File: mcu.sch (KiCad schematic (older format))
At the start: 64 parts, among them J3 SWD, P1 USB_C_Plug_USB2.0, Q1 AO3401A, U10 USBLC6-2SC6, U11 MCP2551-I-SN, U12 STM32F429ZGTx, U8 TPS5430DDA, U9 TPS5430DDA, Y1 25mhz

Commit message: Layout p much finished.. Time for some stretch goals..?
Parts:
- removed C42: 100n, Capacitor_SMD:C_0402_1005Metric_Pad0.74x0.62mm_HandSolder, symbol Device:C_Small
- removed P1: USB_C_Plug_USB2.0, Connector_USB:USB_C_Receptacle_Amphenol_12401548E4-2A, symbol Connector:USB_C_Plug_USB2.0
- removed R48, R51: 5.1k, Resistor_SMD:R_0402_1005Metric_Pad0.72x0.64mm_HandSolder, symbol Device:R_Small
- removed R49, R50: 22, Resistor_SMD:R_0402_1005Metric_Pad0.72x0.64mm_HandSolder, symbol Device:R_Small
- added J4: USB_B, Connector_USB:USB_B_Amphenol_MUSB-D511_Vertical_Rugged, symbol Connector:USB_B
- added J5: USB_EXT, Connector_PinHeader_2.54mm:PinHeader_1x05_P2.54mm_Vertical_SMD_Pin1Left, symbol Connector:Conn_01x05_Male
- added TP18: TP_BUCK_EN, TestPoint:TestPoint_Pad_D1.0mm, symbol Connector:TestPoint_Small
- added TP19: TP_PWR_GND2, TestPoint:TestPoint_Pad_D1.0mm, symbol Connector:TestPoint_Small
- added TP20: TP_PWR_GND1, TestPoint:TestPoint_Pad_D1.0mm, symbol Connector:TestPoint_Small
- added TP21: TP_BUCK_IN, TestPoint:TestPoint_Pad_D1.0mm, symbol Connector:TestPoint_Small
- TP10: value TestPoint_Small -> TP_5V
- TP11: value TestPoint_Small -> TP_3V
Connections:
- net labels added: USB_CONN_SHIELD
- wire segments 230 -> 226
- no-connect marks 3 -> 2

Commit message: Update Schematic with a bunch of extra stuff
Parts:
- added C42, C52: 12p, Capacitor_SMD:C_0402_1005Metric_Pad0.74x0.62mm_HandSolder, symbol Device:C_Small
- added C53: 10u, Capacitor_SMD:C_0402_1005Metric_Pad0.74x0.62mm_HandSolder, symbol Device:C_Small
- added C54: 100n, Capacitor_SMD:C_0402_1005Metric_Pad0.74x0.62mm_HandSolder, symbol Device:C_Small
- added C? (x3): 0.1u, Capacitor_SMD:C_1206_3216Metric_Pad1.33x1.80mm_HandSolder, symbol Device:C_Small
- added C?: 47u, Capacitor_SMD:CP_Elec_5x5.8, symbol Device:CP_Small
- added C?: 10u, Capacitor_Tantalum_SMD:CP_EIA-7343-20_Kemet-V_Pad2.25x2.55mm_HandSolder, symbol Device:CP_Small
- added D22, D25, D26, D27, D28, D29, D30: ESD9B3.3ST5G, Diode_SMD:D_SOD-923, symbol Diode:ESD9B3.3ST5G
- added D23: PWR_5V_GREEN, LED_SMD:LED_0603_1608Metric_Pad1.05x0.95mm_HandSolder, symbol Device:LED_Small
- added D24: PWR_3V_RED, LED_SMD:LED_0603_1608Metric_Pad1.05x0.95mm_HandSolder, symbol Device:LED_Small
- added D? (x2): MM3Zxx, Diode_SMD:D_SOD-323_HandSoldering, symbol Device:D_Small
- added J6: Micro_SD_Card_Det, Connector_Card:microSD_HC_Molex_104031-0811, symbol Connector:Micro_SD_Card_Det
- added J?: HC-05, Connector_PinHeader_2.54mm:PinHeader_1x06_P2.54mm_Vertical, symbol Connector_Generic:Conn_01x06
- added R48: 47, Resistor_SMD:R_0402_1005Metric_Pad0.72x0.64mm_HandSolder, symbol Device:R_Small
- added R49, R74, R75: null, Resistor_SMD:R_0603_1608Metric_Pad0.98x0.95mm_HandSolder, symbol Device:R_Small
- added R50, R51: 4.7k, Resistor_SMD:R_0603_1608Metric_Pad0.98x0.95mm_HandSolder, symbol Device:R_Small
- added R73, R76, R77, R78, R79: 10k, Resistor_SMD:R_0603_1608Metric_Pad0.98x0.95mm_HandSolder, symbol Device:R_Small
- added RV?: Varistor, Varistor:RV_Disc_D15.5mm_W3.9mm_P7.5mm, symbol Device:Varistor
- added TP?: TP_VPROT, TestPoint:TestPoint_Pad_D1.0mm, symbol Connector:TestPoint_Small
- added U16: ATECC608A-SSHDA, Package_SO:SOIC-8_3.9x4.9mm_P1.27mm, symbol Security:ATECC608A-SSHDA
- added Y2: Crystal, Crystal:Crystal_SMD_3215-2Pin_3.2x1.5mm, symbol Device:Crystal
- R53: value 3.24k -> null
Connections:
- net +3V3: now also C54.1, R49.1, R50.2, R51.2, R74.2, R76.2, R77.2, R78.2, R79.2, U16.8 (VCC); no longer C23.1, U11.3 (VDD), U11.5 (Vref)
- net +5V: now also C23.1, U11.3 (VDD), U11.5 (Vref), C?.1, C?.1, C?.1, D?.1 (K), J?.2 (Pin_2), R75.2, TP?.1
- net 12v-SW: now also C?.1, C?.1, D?.2 (A), RV?.2
- net GND: now also C42.2, C52.2, C53.1, C54.2, C?.2, C?.2, C?.2, C?.2, C?.2, D22.2 (A2), D23.1 (K), D24.1 (K), D25.2 (A2), D26.2 (A2), D27.2 (A2), D28.2 (A2), D29.2 (A2), D30.2 (A2), D?.2 (A), J6.6 (VSS), J?.3 (Pin_3), RV?.1, U16.4 (GND)
- net HSE_IN: now also R48.2
- net HSE_OUT: now also C42.1, Y2.1
- net MCU-CLUTCH: now also U12.73 (PB12); no longer U12.76 (PB15)
- net MCU-CRNK: now also U12.118 (PD4); no longer U12.116 (PD2)
- net MCU-IAT: now also U12.46 (PB0); no longer U12.34 (PA0)
- net MCU-IGN-1: now also U12.34 (PA0); no longer U12.96 (PC6)
- net MCU-IGN-2: now also U12.35 (PA1); no longer U12.97 (PC7)
- net MCU-IGN-3: now also U12.69 (PB10); no longer U12.46 (PB0)
- net MCU-IGN-4: now also U12.70 (PB11); no longer U12.47 (PB1)
- net MCU-RN1: now also U12.101 (PA9); no longer U12.69 (PB10)
- net MCU-RN2: now also U12.102 (PA10); no longer U12.70 (PB11)
- net MCU-TPS: now also U12.47 (PB1); no longer U12.35 (PA1)
- net UART7_RX: now also J?.5 (Pin_5)
- net UART7_TX: now also J?.4 (Pin_4)
- net USB_CONN_SHIELD: now also J6.11 (SHIELD)
- net MCU-CEL: now reaches U12.100 (PA8)
- net SDIO_D2: now reaches U12.111 (PC10)
- net SDIO_D2: now also D26.1 (A1), J6.1 (DAT2), R78.1
- net SDIO_D3: now reaches U12.112 (PC11)
- net SDIO_D3: now also D27.1 (A1), J6.2 (DAT3/CD)
- net SDIO_CK: now reaches U12.113 (PC12)
- net SDIO_CK: now also D29.1 (A1), J6.5 (CLK)
- net I2C1_SDL: now reaches U12.136 (PB6)
- net I2C1_SDL: now also R51.1, U16.6 (SCL)
- net I2C1_SDA: now reaches U12.137 (PB7)
- net I2C1_SDA: now also R50.1, U16.5 (SDA)
- net MCU-PWM2: now reaches U12.4 (PE5)
- net MCU-PWM3: now reaches U12.5 (PE6)
- net LSE_IN: now reaches U12.8 (PC14)
- net MCU-VVT: now reaches U12.81 (PD12)
- net MCU-PWM1: now reaches U12.82 (PD13)
- net MCU-ANALOG-1: now reaches U12.87 (PG2)
- net MCU-ANALOG-2: now reaches U12.88 (PG3)
- net MCU-ANALOG-3: now reaches U12.89 (PG4)
- net LSE_OUT: now reaches U12.9 (PC15)
- net MCU-ANALOG-4: now reaches U12.90 (PG5)
- net SDIO_D0: now reaches U12.98 (PC8)
- net SDIO_D0: now also D22.1 (A1), J6.7 (DAT0), R76.1
- net SDIO_D1: now reaches U12.99 (PC9)
- net SDIO_D1: now also D25.1 (A1), J6.8 (DAT1), R77.1
- net MCU-BARO renamed MCU-EXT-MAP
- new net: C52.1, R48.1, Y2.2
- new net: D23.2 (A), R74.1
- new net: D24.2 (A), R75.1
- new net SDIO_CMD: D28.1 (A1), J6.3 (CMD), R73.2, R79.1, U12.116 (PD2)
- new net SDIO_VDD: C53.2, D30.1 (A1), J6.4 (VDD), R49.2, R73.1
- new net VREG: D?.1 (K)
- no-connect marks 2 -> 6
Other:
- note added: "ATECCA"
- note added: "HC-05"
- note added: "POWER LEDS\n"
- note added: "SDCARD + ESD"
- moved on the sheet: C23, C27, C28, C29, C30, C31, C32, C33, C34, C35, C36, C37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

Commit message: Start rerouting again
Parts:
- J4: footprint Connector_USB:USB_B_Amphenol_MUSB-D511_Vertical_Rugged -> Connector_USB:USB_B_Lumberg_2411_02_Horizontal
- gave numbers to parts that had none: 10
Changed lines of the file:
@@
 F 0 "J4" H 1757 7567 50  0000 C CNN
 F 1 "USB_B" H 1757 7476 50  0000 C CNN
-F 2 "Connector_USB:USB_B_Amphenol_MUSB-D511_Vertical_Rugged" H 1850 7050 50  0001 C CNN
+F 2 "Connector_USB:USB_B_Lumberg_2411_02_Horizontal" H 1850 7050 50  0001 C CNN
 F 3 " ~" H 1850 7050 50  0001 C CNN
 	1    1700 7100
@@
 NoConn ~ 13200 5650
 $Comp
-L Connector_Generic:Conn_01x06 J?
+L Connector_Generic:Conn_01x06 J7
 U 1 1 61A6A58F
 P 3250 10850
-F 0 "J?" H 3168 10325 50  0000 C CNN
+F 0 "J7" H 3168 10325 50  0000 C CNN
 F 1 "HC-05" H 3168 10416 50  0000 C CNN
 F 2 "Connector_PinHeader_2.54mm:PinHeader_1x06_P2.54mm_Vertical" H 3250 10850 50  0001 C CNN
@@
 UART7_TX
 $Comp
-L power:GND #PWR?
+L power:GND #PWR092
 U 1 1 61A7105A
 P 3900 10850
-F 0 "#PWR?" H 3900 10600 50  0001 C CNN
+F 0 "#PWR092" H 3900 10600 50  0001 C CNN
 F 1 "GND" H 3905 10677 50  0000 C CNN
 F 2 "" H 3900 10850 50  0001 C CNN
@@
 P 3950 10950
 AR Path="/61A87E29" Ref="#PWR?"  Part="1"
-AR Path="/608F155A/61A87E29" Ref="#PWR?"  Part="1"
-F 0 "#PWR?" H 3950 10800 50  0001 C CNN
+AR Path="/608F155A/61A87E29" Ref="#PWR093"  Part="1"
+F 0 "#PWR093" H 3950 10800 50  0001 C CNN
 F 1 "+5V" V 3950 11050 50  0000 L CNN
 F 2 "" H 3950 10950 50  0001 C CNN
@@
 P 4850 1300
 AR Path="/5F2C75FB/61BA4550" Ref="RV?"  Part="1"
-AR Path="/608F155A/61BA4550" Ref="RV?"  Part="1"
-F 0 "RV?" H 4729 1254 50  0000 R CNN
+AR Path="/608F155A/61BA4550" Ref="RV1"  Part="1"
+F 0 "RV1" H 4729 1254 50  0000 R CNN
 F 1 "Varistor" H 4729 1345 50  0000 R CNN
 F 2 "Varistor:RV_Disc_D15.5mm_W3.9mm_P7.5mm" V 4780 1300 50  0001 C CNN
@@
 P 5650 1350
 AR Path="/5F2C75FB/61BA4558" Ref="C?"  Part="1"
-AR Path="/608F155A/61BA4558" Ref="C?"  Part="1"
-F 0 "C?" H 5742 1396 50  0000 L CNN
+AR Path="/608F155A/61BA4558" Ref="C59"  Part="1"
+F 0 "C59" H 5742 1396 50  0000 L CNN
 F 1 "0.1u" H 5742 1305 50  0000 L CNN
 F 2 "Capacitor_SMD:C_1206_3216Metric_Pad1.33x1.80mm_HandSolder" H 5650 1350 50  0001 C CNN
@@
 P 5950 950
 AR Path="/5F2C75FB/61BA4563" Ref="D?"  Part="1"
-AR Path="/608F155A/61BA4563" Ref="D?"  Part="1"
-F 0 "D?" H 5950 743 50  0000 C CNN
+AR Path="/608F155A/61BA4563" Ref="D35"  Part="1"
+F 0 "D35" H 5950 743 50  0000 C CNN
 F 1 "MM3Zxx" H 5950 834 50  0000 C CNN
 F 2 "Diode_SMD:D_SOD-323_HandSoldering" V 5950 950 50  0001 C CNN
@@
 P 5500 3600
 AR Path="/5F2C75FB/61BA4578" Ref="C?"  Part="1"
-AR Path="/608F155A/61BA4578" Ref="C?"  Part="1"
-F 0 "C?" H 5592 3646 50  0000 L CNN
+AR Path="/608F155A/61BA4578" Ref="C58"  Part="1"
+F 0 "C58" H 5592 3646 50  0000 L CNN
 F 1 "0.1u" H 5592 3555 50  0000 L CNN
 F 2 "Capacitor_SMD:C_1206_3216Metric_Pad1.33x1.80mm_HandSolder" H 5500 3600 50  0001 C CNN
@@
 P 5150 3550
 AR Path="/5F2C75FB/61BA4580" Ref="C?"  Part="1"
-AR Path="/608F155A/61BA4580" Ref="C?"  Part="1"
-F 0 "C?" H 5238 3596 50  0000 L CNN
+AR Path="/608F155A/61BA4580" Ref="C56"  Part="1"
+F 0 "C56" H 5238 3596 50  0000 L CNN
 F 1 "47u" H 5238 3505 50  0000 L CNN
 F 2 "Capacitor_SMD:CP_Elec_5x5.8" H 5150 3550 50  0001 C CNN
@@
 P 4700 3550
 AR Path="/5F2C75FB/61BA4588" Ref="D?"  Part="1"
-AR Path="/608F155A/61BA4588" Ref="D?"  Part="1"
-F 0 "D?" V 4654 3620 50  0000 L CNN
+AR Path="/608F155A/61BA4588" Ref="D34"  Part="1"
+F 0 "D34" V 4654 3620 50  0000 L CNN
 F 1 "MM3Zxx" V 4745 3620 50  0000 L CNN
 F 2 "Diode_SMD:D_SOD-323_HandSoldering" V 4700 3550 50  0001 C CNN
@@
 P 5350 1350
 AR Path="/5F2C75FB/61BA459E" Ref="C?"  Part="1"
-AR Path="/608F155A/61BA459E" Ref="C?"  Part="1"
-F 0 "C?" H 5438 1396 50  0000 L CNN
+AR Path="/608F155A/61BA459E" Ref="C57"  Part="1"
+F 0 "C57" H 5438 1396 50  0000 L CNN
 F 1 "10u" H 5438 1305 50  0000 L CNN
 F 2 "Capacitor_Tantalum_SMD:CP_EIA-7343-20_Kemet-V_Pad2.25x2.55mm_HandSolder" H 5350 1350 50  0001 C CNN
@@
 P 5850 3600
 AR Path="/5F2C75FB/61BA45A9" Ref="C?"  Part="1"
-AR Path="/608F155A/61BA45A9" Ref="C?"  Part="1"
-F 0 "C?" H 5942 3646 50  0000 L CNN
+AR Path="/608F155A/61BA45A9" Ref="C60"  Part="1"
+F 0 "C60" H 5942 3646 50  0000 L CNN
 F 1 "0.1u" H 5942 3555 50  0000 L CNN
 F 2 "Capacitor_SMD:C_1206_3216Metric_Pad1.33x1.80mm_HandSolder" H 5850 3600 50  0001 C CNN
@@
 P 5850 3200
 AR Path="/5F2C75FB/61BA45B5" Ref="TP?"  Part="1"
-AR Path="/608F155A/61BA45B5" Ref="TP?"  Part="1"
-F 0 "TP?" H 5898 3246 50  0000 L CNN
+AR Path="/608F155A/61BA45B5" Ref="TP22"  Part="1"
+F 0 "TP22" H 5898 3246 50  0000 L CNN
 F 1 "TP_VPROT" H 5898 3155 50  0000 L CNN
 F 2 "TestPoint:TestPoint_Pad_D1.0mm" H 6050 3200 50  0001 C CNN
@@
 P 4300 1550
 AR Path="/5F2C75FB/61BA45BF" Ref="#PWR?"  Part="1"
-AR Path="/608F155A/61BA45BF" Ref="#PWR?"  Part="1"
-F 0 "#PWR?" H 4300 1300 50  0001 C CNN
+AR Path="/608F155A/61BA45BF" Ref="#PWR094"  Part="1"
+F 0 "#PWR094" H 4300 1300 50  0001 C CNN
 F 1 "GND" H 4305 1377 50  0000 C CNN
 F 2 "" H 4300 1550 50  0001 C CNN
@@
 P 4700 3400
 AR Path="/61D409BC" Ref="#PWR?"  Part="1"
-AR Path="/608F155A/61D409BC" Ref="#PWR?"  Part="1"
-F 0 "#PWR?" H 4700 3250 50  0001 C CNN
+AR Path="/608F155A/61D409BC" Ref="#PWR095"  Part="1"
+F 0 "#PWR095" H 4700 3250 50  0001 C CNN
 F 1 "+5V" V 4700 3500 50  0000 L CNN
 F 2 "" H 4700 3400 50  0001 C CNN
@@
 	4700 3650 4700 3800
 $Comp
-L power:GND #PWR?
+L power:GND #PWR096
 U 1 1 61D4331B
 P 4700 3800
-F 0 "#PWR?" H 4700 3550 50  0001 C CNN
+F 0 "#PWR096" H 4700 3550 50  0001 C CNN
 F 1 "GND" H 4705 3627 50  0000 C CNN
 F 2 "" H 4700 3800 50  0001 C CNN

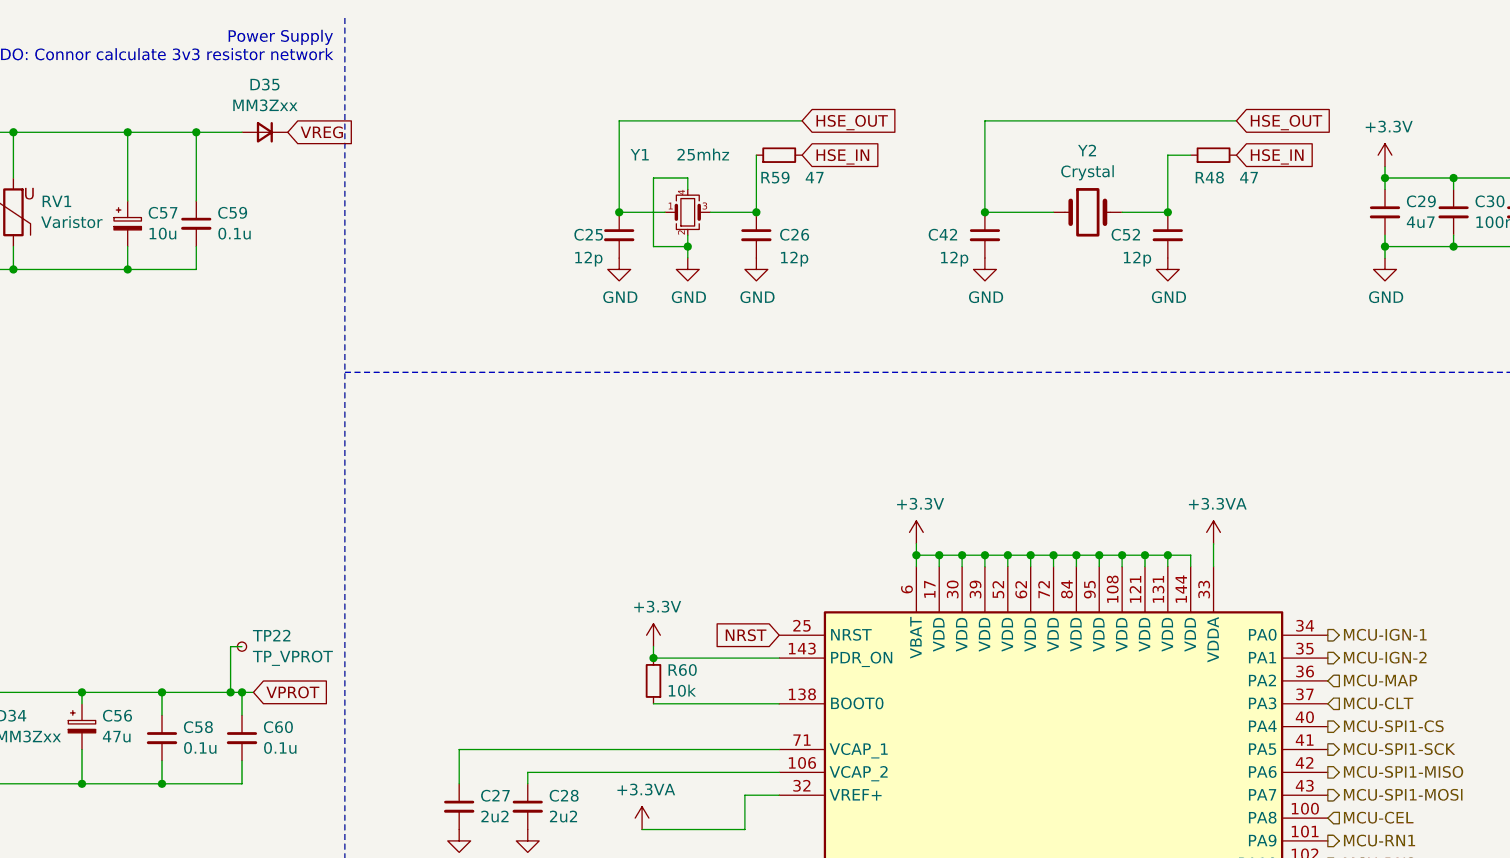
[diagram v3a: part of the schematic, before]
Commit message: Layout checkpoint: everything fits on the board
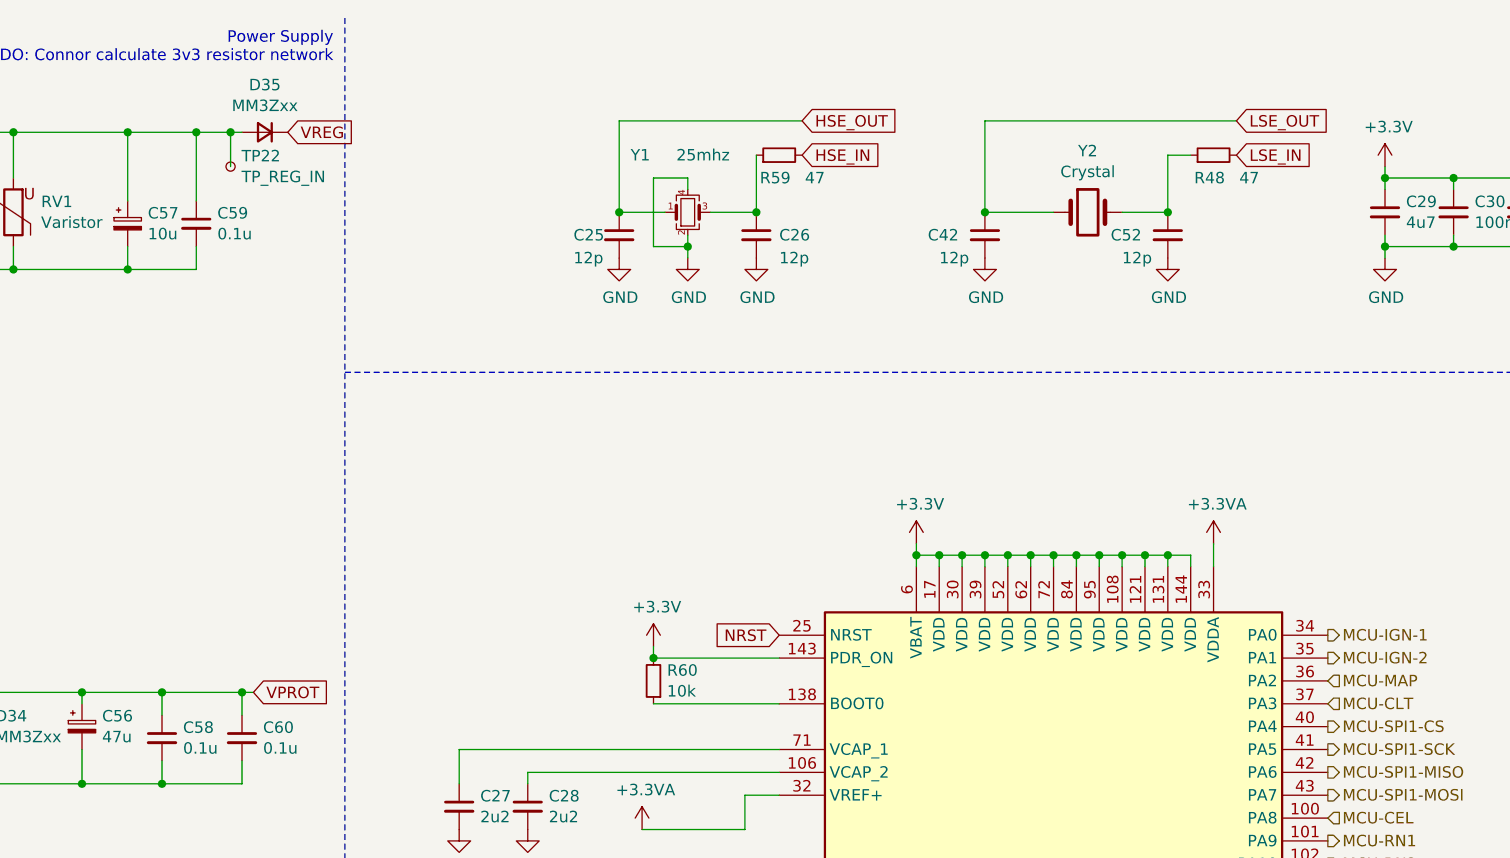
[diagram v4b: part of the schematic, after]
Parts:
- TP22: value TP_VPROT -> TP_REG_IN
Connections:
- net +5V: no longer TP22.1
- net 12v-SW: now also TP22.1
- net HSE_IN: no longer R48.2
- net HSE_OUT: no longer C42.1, Y2.1
- net LSE_IN: now also R48.2
- net LSE_OUT: now also C42.1, Y2.1
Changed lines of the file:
@@
 	9100 1300 9400 1300
 Text GLabel 10200 900  2    50   Input ~ 0
-HSE_OUT
+LSE_OUT
 Text GLabel 10200 1050 2    50   Input ~ 0
-HSE_IN
+LSE_IN
 $Comp
 L Device:R_Small R48
@@
 Connection ~ 5350 950
 Wire Wire Line
-	5650 950  5850 950
+	5650 950  5800 950
 Connection ~ 5650 950
 Text GLabel 6050 950  2    50   Input ~ 0
@@
 Wire Wire Line
 	4350 950  4850 950
-Wire Wire Line
-	5500 3400 5800 3400
 $Comp
 L Device:C_Small C?
@@
 Connection ~ 5500 3800
 $Comp
-L Connector:TestPoint_Small TP?
-U 1 1 61BA45B5
-P 5850 3200
-AR Path="/5F2C75FB/61BA45B5" Ref="TP?"  Part="1"
-AR Path="/608F155A/61BA45B5" Ref="TP22"  Part="1"
-F 0 "TP22" H 5898 3246 50  0000 L CNN
-F 1 "TP_VPROT" H 5898 3155 50  0000 L CNN
-F 2 "TestPoint:TestPoint_Pad_D1.0mm" H 6050 3200 50  0001 C CNN
-F 3 "~" H 6050 3200 50  0001 C CNN
-	1    5850 3200
-	1    0    0    -1
-$EndComp
-Wire Wire Line
-	5850 3200 5800 3200
-Wire Wire Line
-	5800 3200 5800 3400
-Connection ~ 5800 3400
-Wire Wire Line
-	5800 3400 5850 3400
-$Comp
 L power:GND #PWR?
 U 1 1 61BA45BF
@@
 $EndComp
 Connection ~ 4700 3800
+Wire Wire Line
+	5500 3400 5850 3400
+Wire Wire Line
+	5800 1100 5800 950
+Connection ~ 5800 950
+Wire Wire Line
+	5800 950  5850 950
+$Comp
+L Connector:TestPoint_Small TP22
+U 1 1 609C74ED
+P 5800 1100
+F 0 "TP22" H 5848 1146 50  0000 L CNN
+F 1 "TP_REG_IN" H 5848 1055 50  0000 L CNN
+F 2 "TestPoint:TestPoint_Pad_D1.0mm" H 6000 1100 50  0001 C CNN
+F 3 "~" H 6000 1100 50  0001 C CNN
+	1    5800 1100
+	1    0    0    -1
+$EndComp
 $EndSCHEMATC

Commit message: Finish reroute again
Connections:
- net +3V3: no longer R76.2, R77.2, R78.2, R79.2
- net MCU-PWM2: now also U12.5 (PE6); no longer U12.4 (PE5)
- net MCU-PWM3: now also U12.4 (PE5); no longer U12.5 (PE6)
- net SDIO_VDD: now also R76.2, R77.2, R78.2, R79.2
- net USB_CONN_SHIELD: no longer J6.11 (SHIELD)
- net MCU-EXT-MAP: no longer names the net of U12.45 (PC5)
- no-connect marks 6 -> 7
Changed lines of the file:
@@
 Text GLabel 8200 7250 0    50   Output ~ 0
 UART7_TX
-Text HLabel 10600 7050 2    50   Input ~ 0
-MCU-EXT-MAP
 Text HLabel 10600 6150 2    50   Input ~ 0
 MCU-AC
@@
 Text HLabel 10600 9550 2    50   Input ~ 0
 MCU-PWM1
+Text HLabel 8200 8850 0    50   Input ~ 0
+MCU-PWM2
 Text HLabel 8200 8750 0    50   Input ~ 0
-MCU-PWM2
-Text HLabel 8200 8850 0    50   Input ~ 0
 MCU-PWM3
 $Comp
@@
 	-1   0    0    1
 $EndComp
-$Comp
-L power:+3.3V #PWR0109
-U 1 1 60D55F7E
-P 15050 4400
-F 0 "#PWR0109" H 15050 4250 50  0001 C CNN
-F 1 "+3.3V" H 15065 4573 50  0000 C CNN
-F 2 "" H 15050 4400 50  0001 C CNN
-F 3 "" H 15050 4400 50  0001 C CNN
-	1    15050 4400
-	1    0    0    -1
-$EndComp
 Wire Wire Line
 	15050 4400 15050 4550
@@
 Wire Wire Line
 	15550 4550 15800 4550
-Text GLabel 14900 5650 2    50   UnSpc ~ 0
-USB_CONN_SHIELD
 $Comp
 L Diode:ESD9B3.3ST5G D22
@@
 	1    0    0    -1
 $EndComp
+Text GLabel 15050 4400 1    50   Output ~ 0
+SDIO_VDD
+NoConn ~ 14900 5650
 $EndSCHEMATC
